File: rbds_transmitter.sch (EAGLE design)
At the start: 74 parts, among them IC1 MAX1551, IC2 TPS61030, IC3 MCP4812, IC4 OPA4743UA, IC5 OPA4743UA, Q1 P-Ch, SW1 FSMSM, U3 ATMEGA328, X1 HD44780LCD-1602, Y1 16Mhz

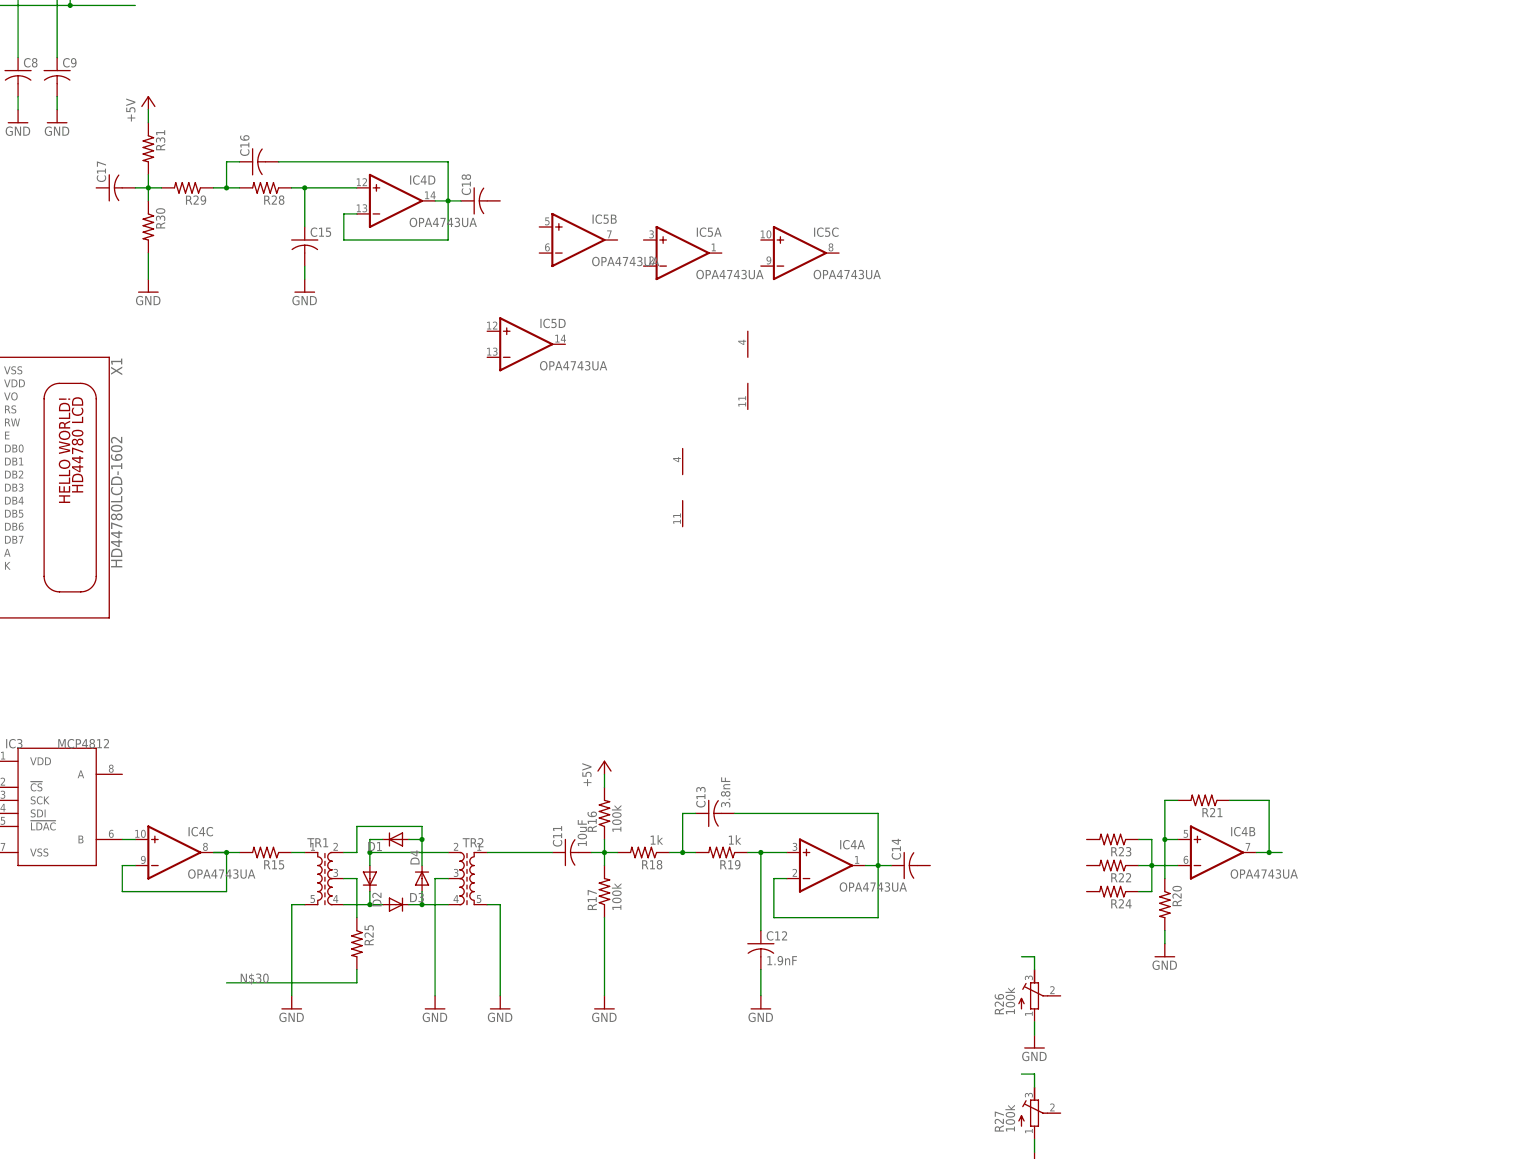
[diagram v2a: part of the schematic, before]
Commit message: more filters
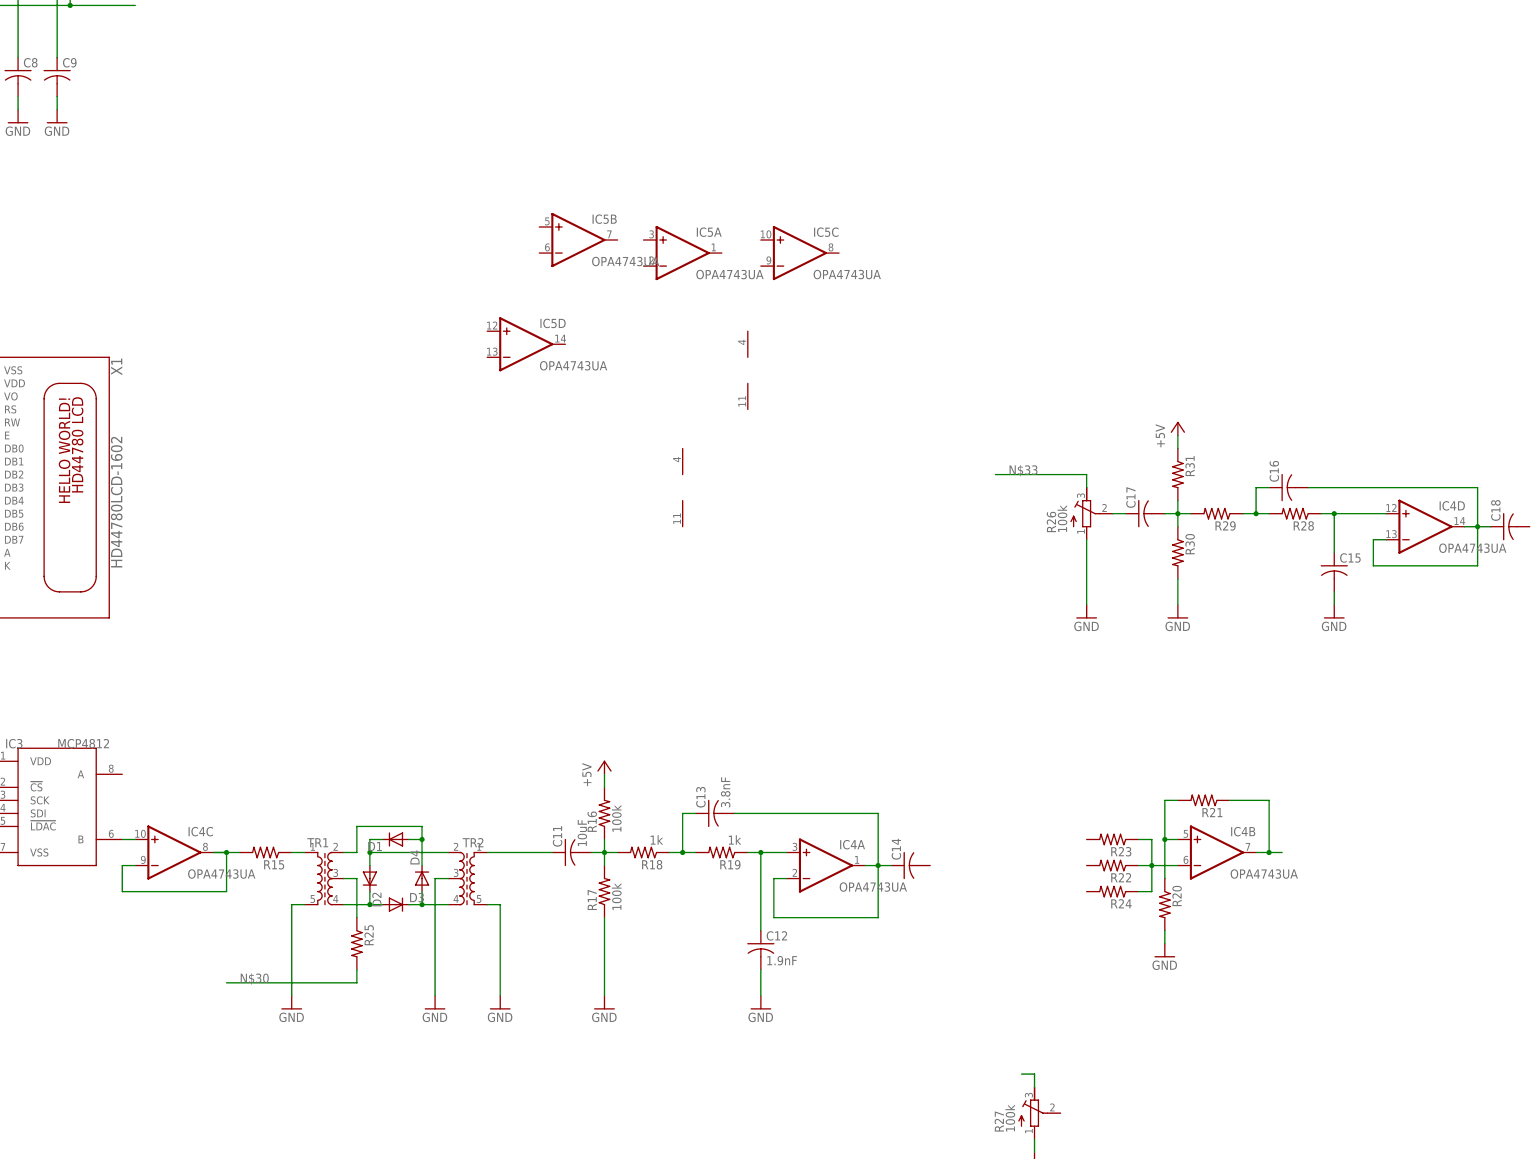
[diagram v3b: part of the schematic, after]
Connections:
- new net N$37: C17.1, R26.S
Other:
- moved on the sheet: C15, C16, C17, C18, IC4D, R26, R28, R29, R30, R31
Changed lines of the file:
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@@
 <instance part="IC4" gate="B" x="419.1" y="-30.48"/>
 <instance part="IC4" gate="C" x="215.9" y="-30.48"/>
-<instance part="IC4" gate="D" x="259.08" y="96.52"/>
+<instance part="IC4" gate="D" x="459.74" y="33.02"/>
 <instance part="IC4" gate="P" x="314.96" y="40.64"/>
 <instance part="R16" gate="G$1" x="299.72" y="-22.86" rot="R90"/>
@@
 <instance part="GND27" gate="1" x="330.2" y="-60.96"/>
 <instance part="C13" gate="G$1" x="320.04" y="-22.86" rot="R90"/>
-<instance part="R26" gate="G$1" x="383.54" y="-58.42"/>
+<instance part="R26" gate="G$1" x="393.7" y="35.56"/>
 <instance part="R27" gate="G$1" x="383.54" y="-81.28"/>
 <instance part="GND29" gate="1" x="383.54" y="-91.44"/>
-<instance part="GND30" gate="1" x="383.54" y="-68.58"/>
+<instance part="GND30" gate="1" x="393.7" y="15.24"/>
 <instance part="IC5" gate="D" x="284.48" y="68.58"/>
 <instance part="IC5" gate="A" x="314.96" y="86.36"/>
@@
 <instance part="IC5" gate="P" x="327.66" y="63.5"/>
 <instance part="C14" gate="G$1" x="358.14" y="-33.02" rot="R90"/>
-<instance part="C15" gate="G$1" x="241.3" y="88.9"/>
-<instance part="C16" gate="G$1" x="231.14" y="104.14" rot="R90"/>
-<instance part="C17" gate="G$1" x="203.2" y="99.06" rot="R90"/>
-<instance part="C18" gate="G$1" x="274.32" y="96.52" rot="R90"/>
-<instance part="R28" gate="G$1" x="233.68" y="99.06" rot="R180"/>
-<instance part="R29" gate="G$1" x="218.44" y="99.06" rot="R180"/>
-<instance part="R30" gate="G$1" x="210.82" y="91.44" rot="R270"/>
-<instance part="R31" gate="G$1" x="210.82" y="106.68" rot="R270"/>
-<instance part="GND31" gate="1" x="210.82" y="78.74"/>
-<instance part="GND32" gate="1" x="241.3" y="78.74"/>
-<instance part="P+10" gate="1" x="210.82" y="116.84"/>
+<instance part="C15" gate="G$1" x="441.96" y="25.4"/>
+<instance part="C16" gate="G$1" x="431.8" y="40.64" rot="R90"/>
+<instance part="C17" gate="G$1" x="403.86" y="35.56" rot="R90"/>
+<instance part="C18" gate="G$1" x="474.98" y="33.02" rot="R90"/>
+<instance part="R28" gate="G$1" x="434.34" y="35.56" rot="R180"/>
+<instance part="R29" gate="G$1" x="419.1" y="35.56" rot="R180"/>
+<instance part="R30" gate="G$1" x="411.48" y="27.94" rot="R270"/>
+<instance part="R31" gate="G$1" x="411.48" y="43.18" rot="R270"/>
+<instance part="GND31" gate="1" x="411.48" y="15.24"/>
+<instance part="GND32" gate="1" x="441.96" y="15.24"/>
+<instance part="P+10" gate="1" x="411.48" y="53.34"/>
 </instances>
 <busses>
@@
 <pinref part="GND30" gate="1" pin="GND"/>
 <pinref part="R26" gate="G$1" pin="A"/>
-<wire x1="383.54" y1="-63.5" x2="383.54" y2="-66.04" width="0.1524" layer="91"/>
+<wire x1="393.7" y1="30.48" x2="393.7" y2="17.78" width="0.1524" layer="91"/>
 </segment>
 <segment>
@@
 <pinref part="C15" gate="G$1" pin="2"/>
 <pinref part="GND32" gate="1" pin="GND"/>
-<wire x1="241.3" y1="81.28" x2="241.3" y2="83.82" width="0.1524" layer="91"/>
+<wire x1="441.96" y1="17.78" x2="441.96" y2="20.32" width="0.1524" layer="91"/>
 </segment>
 <segment>
 <pinref part="R30" gate="G$1" pin="2"/>
 <pinref part="GND31" gate="1" pin="GND"/>
-<wire x1="210.82" y1="81.28" x2="210.82" y2="86.36" width="0.1524" layer="91"/>
+<wire x1="411.48" y1="17.78" x2="411.48" y2="22.86" width="0.1524" layer="91"/>
 </segment>
 </net>
@@
 <pinref part="R31" gate="G$1" pin="1"/>
 <pinref part="P+10" gate="1" pin="+5V"/>
-<wire x1="210.82" y1="114.3" x2="210.82" y2="111.76" width="0.1524" layer="91"/>
+<wire x1="411.48" y1="50.8" x2="411.48" y2="48.26" width="0.1524" layer="91"/>
 </segment>
 </net>
@@
 <segment>
 <pinref part="R26" gate="G$1" pin="E"/>
-<wire x1="383.54" y1="-53.34" x2="383.54" y2="-50.8" width="0.1524" layer="91"/>
-<wire x1="383.54" y1="-50.8" x2="381" y2="-50.8" width="0.1524" layer="91"/>
+<wire x1="393.7" y1="40.64" x2="393.7" y2="43.18" width="0.1524" layer="91"/>
+<wire x1="393.7" y1="43.18" x2="375.92" y2="43.18" width="0.1524" layer="91"/>
+<label x="378.46" y="43.18" size="1.778" layer="95"/>
 </segment>
 </net>
@@
 <pinref part="IC4" gate="D" pin="+IN"/>
 <pinref part="R28" gate="G$1" pin="1"/>
-<wire x1="238.76" y1="99.06" x2="241.3" y2="99.06" width="0.1524" layer="91"/>
+<wire x1="439.42" y1="35.56" x2="441.96" y2="35.56" width="0.1524" layer="91"/>
 <pinref part="C15" gate="G$1" pin="1"/>
-<wire x1="241.3" y1="99.06" x2="251.46" y2="99.06" width="0.1524" layer="91"/>
-<wire x1="241.3" y1="91.44" x2="241.3" y2="99.06" width="0.1524" layer="91"/>
-<junction x="241.3" y="99.06"/>
+<wire x1="441.96" y1="35.56" x2="452.12" y2="35.56" width="0.1524" layer="91"/>
+<wire x1="441.96" y1="27.94" x2="441.96" y2="35.56" width="0.1524" layer="91"/>
+<junction x="441.96" y="35.56"/>
 </segment>
 </net>
@@
 <segment>
 <pinref part="IC4" gate="D" pin="-IN"/>
-<wire x1="251.46" y1="93.98" x2="248.92" y2="93.98" width="0.1524" layer="91"/>
-<wire x1="248.92" y1="93.98" x2="248.92" y2="88.9" width="0.1524" layer="91"/>
-<wire x1="248.92" y1="88.9" x2="269.24" y2="88.9" width="0.1524" layer="91"/>
-<wire x1="269.24" y1="88.9" x2="269.24" y2="96.52" width="0.1524" layer="91"/>
+<wire x1="452.12" y1="30.48" x2="449.58" y2="30.48" width="0.1524" layer="91"/>
+<wire x1="449.58" y1="30.48" x2="449.58" y2="25.4" width="0.1524" layer="91"/>
+<wire x1="449.58" y1="25.4" x2="469.9" y2="25.4" width="0.1524" layer="91"/>
+<wire x1="469.9" y1="25.4" x2="469.9" y2="33.02" width="0.1524" layer="91"/>
 <pinref part="IC4" gate="D" pin="OUT"/>
-<wire x1="269.24" y1="96.52" x2="266.7" y2="96.52" width="0.1524" layer="91"/>
+<wire x1="469.9" y1="33.02" x2="467.36" y2="33.02" width="0.1524" layer="91"/>
 <pinref part="C16" gate="G$1" pin="2"/>
-<wire x1="236.22" y1="104.14" x2="269.24" y2="104.14" width="0.1524" layer="91"/>
-<wire x1="269.24" y1="104.14" x2="269.24" y2="96.52" width="0.1524" layer="91"/>
-<junction x="269.24" y="96.52"/>
+<wire x1="436.88" y1="40.64" x2="469.9" y2="40.64" width="0.1524" layer="91"/>
+<wire x1="469.9" y1="40.64" x2="469.9" y2="33.02" width="0.1524" layer="91"/>
+<junction x="469.9" y="33.02"/>
 <pinref part="C18" gate="G$1" pin="1"/>
-<wire x1="271.78" y1="96.52" x2="269.24" y2="96.52" width="0.1524" layer="91"/>
+<wire x1="472.44" y1="33.02" x2="469.9" y2="33.02" width="0.1524" layer="91"/>
 </segment>
 </net>
@@
 <segment>
 <pinref part="R28" gate="G$1" pin="2"/>
-<wire x1="228.6" y1="99.06" x2="226.06" y2="99.06" width="0.1524" layer="91"/>
-<wire x1="226.06" y1="99.06" x2="226.06" y2="104.14" width="0.1524" layer="91"/>
+<wire x1="429.26" y1="35.56" x2="426.72" y2="35.56" width="0.1524" layer="91"/>
+<wire x1="426.72" y1="35.56" x2="426.72" y2="40.64" width="0.1524" layer="91"/>
 <pinref part="C16" gate="G$1" pin="1"/>
-<wire x1="226.06" y1="104.14" x2="228.6" y2="104.14" width="0.1524" layer="91"/>
-<junction x="226.06" y="99.06"/>
+<wire x1="426.72" y1="40.64" x2="429.26" y2="40.64" width="0.1524" layer="91"/>
+<junction x="426.72" y="35.56"/>
 <pinref part="R29" gate="G$1" pin="1"/>
-<wire x1="223.52" y1="99.06" x2="226.06" y2="99.06" width="0.1524" layer="91"/>
+<wire x1="424.18" y1="35.56" x2="426.72" y2="35.56" width="0.1524" layer="91"/>
 </segment>
 </net>
@@
 <pinref part="R30" gate="G$1" pin="1"/>
 <pinref part="R31" gate="G$1" pin="2"/>
-<wire x1="210.82" y1="96.52" x2="210.82" y2="99.06" width="0.1524" layer="91"/>
+<wire x1="411.48" y1="33.02" x2="411.48" y2="35.56" width="0.1524" layer="91"/>
 <pinref part="R29" gate="G$1" pin="2"/>
-<wire x1="210.82" y1="99.06" x2="210.82" y2="101.6" width="0.1524" layer="91"/>
-<wire x1="213.36" y1="99.06" x2="210.82" y2="99.06" width="0.1524" layer="91"/>
+<wire x1="411.48" y1="35.56" x2="411.48" y2="38.1" width="0.1524" layer="91"/>
+<wire x1="414.02" y1="35.56" x2="411.48" y2="35.56" width="0.1524" layer="91"/>
 <pinref part="C17" gate="G$1" pin="2"/>
-<wire x1="208.28" y1="99.06" x2="210.82" y2="99.06" width="0.1524" layer="91"/>
-<junction x="210.82" y="99.06"/>
-</segment>
-</net>
+<wire x1="408.94" y1="35.56" x2="411.48" y2="35.56" width="0.1524" layer="91"/>
+<junction x="411.48" y="35.56"/>
+</segment>
+</net>
+<net name="N$37" class="0">
+<segment>
+<pinref part="C17" gate="G$1" pin="1"/>
+<pinref part="R26" gate="G$1" pin="S"/>
+<wire x1="398.78" y1="35.56" x2="401.32" y2="35.56" width="0.1524" layer="91"/>
+</segment>
+</net>

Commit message: yet more filters
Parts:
- added C19, C20, C21, C22: (no value), adafruit:C-USC1206
- added R32, R33, R34, R35, R37: (no value), adafruit:R-US_R1206
- added R36: 100k, rcl:R-TRIMM4G/J
- added S1: (no value), sparkfun:SWITCH-SPSTSMD2
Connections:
- removed net N$32 (its old number): R27.E
- new net N$37: C21.1, R36.S
- new net N$39: C19.1, C22.2, IC5A.-IN, IC5A.OUT
- new net N$40: C20.1, IC5A.+IN, R35.2
- new net N$41: C22.1, R34.2, R35.1
- new net N$42: R36.E
- new net N$43: C21.2, R32.2, R33.1, R34.1
- new net N$44: C14.2, R23.2
- new net N$45: C19.2, R22.2
- new net N$46: IC3.A, IC5B.+IN
- new net N$47: IC5B.-IN, IC5B.OUT, R37.2
- new net N$48: C18.2, R24.2
- new net N$49: C11.1, R27.S
- new net N$50: C7.1, C8.1, C9.1, IC2.VOUT@0, IC2.VOUT@1, IC2.VOUT@2, R11.2, R9.2, S1.S
- net +5V: now also R32.1, S1.P; no longer C7.1, C8.1, C9.1, IC2.VOUT@0, IC2.VOUT@1, IC2.VOUT@2, R11.2, R9.2
- net GND: now also C20.2, R33.2, R36.A
- net N$21: now also R27.E; no longer C11.1
- net N$27: now also R37.1
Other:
- moved on the sheet: C1, C10, C11, C12, C13, C14, C15, C16, C17, C18, C3, C31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

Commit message: seperated out some parts
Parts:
- added C23, C24, C25, C26, C27, C28, C29, C30, C32: (no value), adafruit:C-USC1206
- added R38, R39, R40, R41: (no value), adafruit:R-US_R1206
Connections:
- net N$10 renamed LOWBAT
- net N$29 renamed BPSK
- net N$33 renamed TONE
- net N$42 renamed PILOT
- net N$47 renamed FREQUENCY
- new net CARRIER: C26.1
- new net N$42: C23.1, R38.1, R39.2
- new net N$47: C24.1, IC5C.+IN, R39.1
- new net N$51: C26.2, R38.2, R40.1, R41.2
- new net N$53: C25.2, R25.1
- new net RBDS: R27.E, TR2.3
- net +5V: now also C28.1, C29.1, C30.1, C32.1, C7.1, C8.1, C9.1, IC2.VOUT@0, IC2.VOUT@1, IC2.VOUT@2, IC4P.V+, IC5P.V+, R11.2, R41.1, R9.2; no longer S1.P
- net GND: now also C24.2, C28.2, C29.2, C30.2, C32.2, IC4P.V-, IC5P.V-, R40.2, TR1.3, TR2.1; no longer TR2.3, TR2.5
- net N$11: now also S1.O; no longer IC2.EN, IC2.VBAT, L1.1, R7.2
- net N$14: now also D3.C, D4.A, TR2.2; no longer D1.A, D4.C, TR1.2
- net N$16: now also D3.A, TR1.2; no longer D2.A, TR2.2
- net N$18: now also D2.A, D4.C; no longer D2.C, D3.A
- net N$19: now also R25.2, TR2.5; no longer R25.1, TR1.3
- net N$21: now also C27.2; no longer R27.E, TR2.1
- net N$26: now also C27.1
- net N$3: now also D1.A, D2.C; no longer D3.C, D4.A
- net N$30: now also C23.2, C25.1, IC5C.-IN, IC5C.OUT; no longer R25.2
- net N$50: now also IC2.EN, IC2.VBAT, L1.1, R7.2, S1.P; no longer C7.1, C8.1, C9.1, IC2.VOUT@0, IC2.VOUT@1, IC2.VOUT@2, R11.2, R9.2, S1.S
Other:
- moved on the sheet: C10, C11, C12, C13, C14, C15, C16, C17, C18, C19, C2, C20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

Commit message: fixed up usb charger for load switching, worked some on op amps
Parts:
- removed JP2: (no value), sparkfun:M02PTH
- removed LED1: (no value), adafruit:LEDCHIPLED_1206
- added D6: (no value), adafruit:DIODESMA
- added Q2: P-CH, sparkfun:MOSFET-PCHANNELSMD
- R5: value 10k -> (none)
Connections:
- removed net N$5: IC1.!POK, LED1.C
- new net N$10: IC1.!POK, Q2.G, R5.2
- net GND: no longer JP2.2
- net N$1: now also D6.A
- net N$11: now also Q2.D, R5.1; no longer JP2.1, R5.2, S1.O
- net N$23: now also IC4B.-IN; no longer IC4B.+IN
- net N$27: now also IC4B.+IN; no longer IC4B.-IN
- net N$6: now also D6.C, Q2.S, S1.S; no longer LED1.A, R5.1
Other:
- moved on the sheet: C2, C23, C24, C25, C26, C27, C4, C7, C8, C9, CN1, D1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

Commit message: still working
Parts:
- added C33: (no value), adafruit:C-USC1206
- added R42, R43: (no value), adafruit:R-US_R1206
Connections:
- new net GNDA: IC5D.-IN, IC5D.OUT
- new net N$29: C33.1, IC5D.+IN, R42.2, R43.1
- new net N$5: R37.1
- net +5V: now also R42.1
- net GND: now also C33.2, R43.2
- net N$27: no longer IC4B.+IN, R37.1
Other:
- moved on the sheet: C27, IC4B, IC5D, R20, R21, R22, R23, R24

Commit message: adding tx
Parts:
- removed C33: (no value), adafruit:C-USC1206
- added ANT1, ANT2: (no value), discrete:ANTENNA
- added C34, C35, C36, C37: (no value), adafruit:C-USC1206
- added IC6: MAX2606, maxim:MAX2606
- added L2, L4: (no value), resistor:L-USL1812
- added R44, R45: (no value), adafruit:R-US_R1206
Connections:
- net GNDA renamed N$55
- new net N$33: C19.1, IC6.OUT+, R44.2
- new net N$52: ANT2.1, C34.2
- new net N$54: CN1.VBUS, L4.1
- new net N$56: C36.2, R22.2
- new net N$57: C35.2, R23.2
- new net N$58: R42.1
- net +5V: now also C14.1, C18.1, IC6.VCC, R44.1, R45.1; no longer R42.1
- net GND: now also C14.2, C18.2, IC5D.+IN, IC6.GND, L2.1, R43.1; no longer C33.2, R43.2
- net N$1: now also L4.2; no longer CN1.VBUS
- net N$24: now also IC6.IND, L2.2; no longer C13.2, C14.1, IC4A.-IN, IC4A.OUT
- net N$27: now also IC6.TUNE, R42.2, R43.2; no longer R22.1, R23.1, R24.1
- net N$29: now also C16.2, C37.1, IC4D.-IN, IC4D.OUT; no longer C33.1, IC5D.+IN, R42.2, R43.1
- net N$35: now also C34.1, IC6.OUT-, R45.2; no longer C16.2, C18.1, IC4D.-IN, IC4D.OUT
- net N$39: now also ANT1.1, C19.2; no longer C19.1, C22.2, IC5A.-IN, IC5A.OUT
- net N$44: now also C13.2, C35.1, IC4A.-IN, IC4A.OUT; no longer C14.2, R23.2
- net N$45: now also C22.2, C36.1, IC5A.-IN, IC5A.OUT; no longer C19.2, R22.2
- net N$48: now also C37.2; no longer C18.2
- net N$5: now also IC4B.+IN, R22.1, R23.1, R24.1
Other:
- moved on the sheet: C11, C12, C13, C14, C15, C16, C17, C18, C19, C20, C21, C22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
